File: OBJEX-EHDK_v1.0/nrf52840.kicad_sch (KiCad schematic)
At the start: 21 parts, among them U6 nRF52840, Y2 32MHz, Y3 32.768kHz

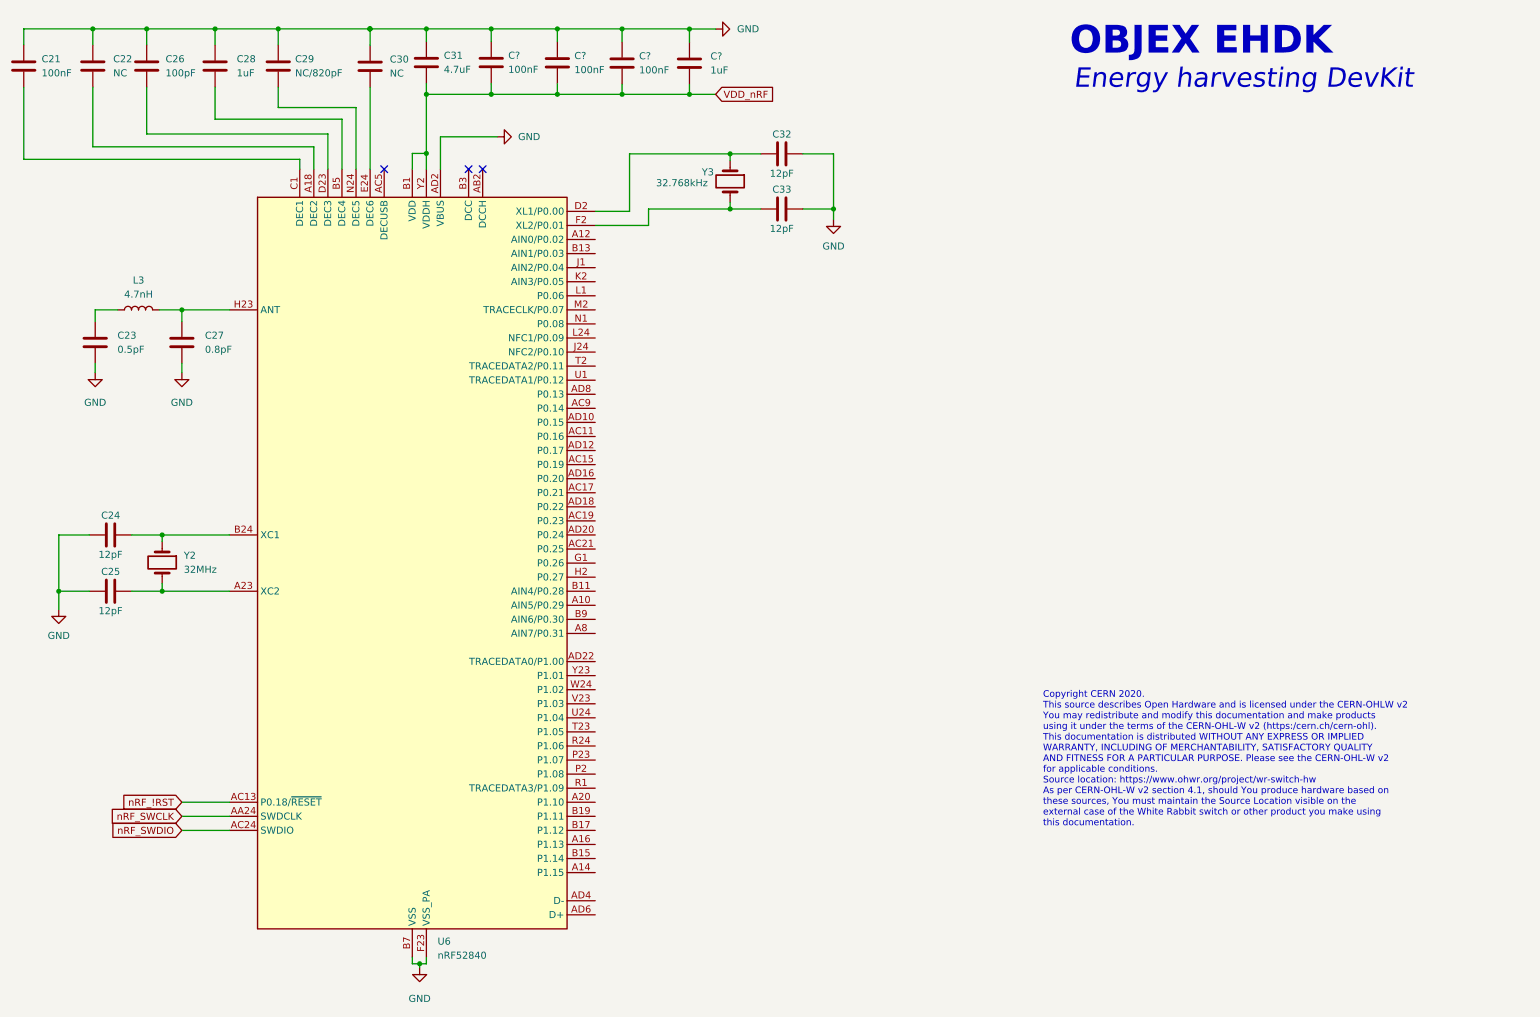
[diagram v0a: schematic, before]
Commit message: add: ADP5091
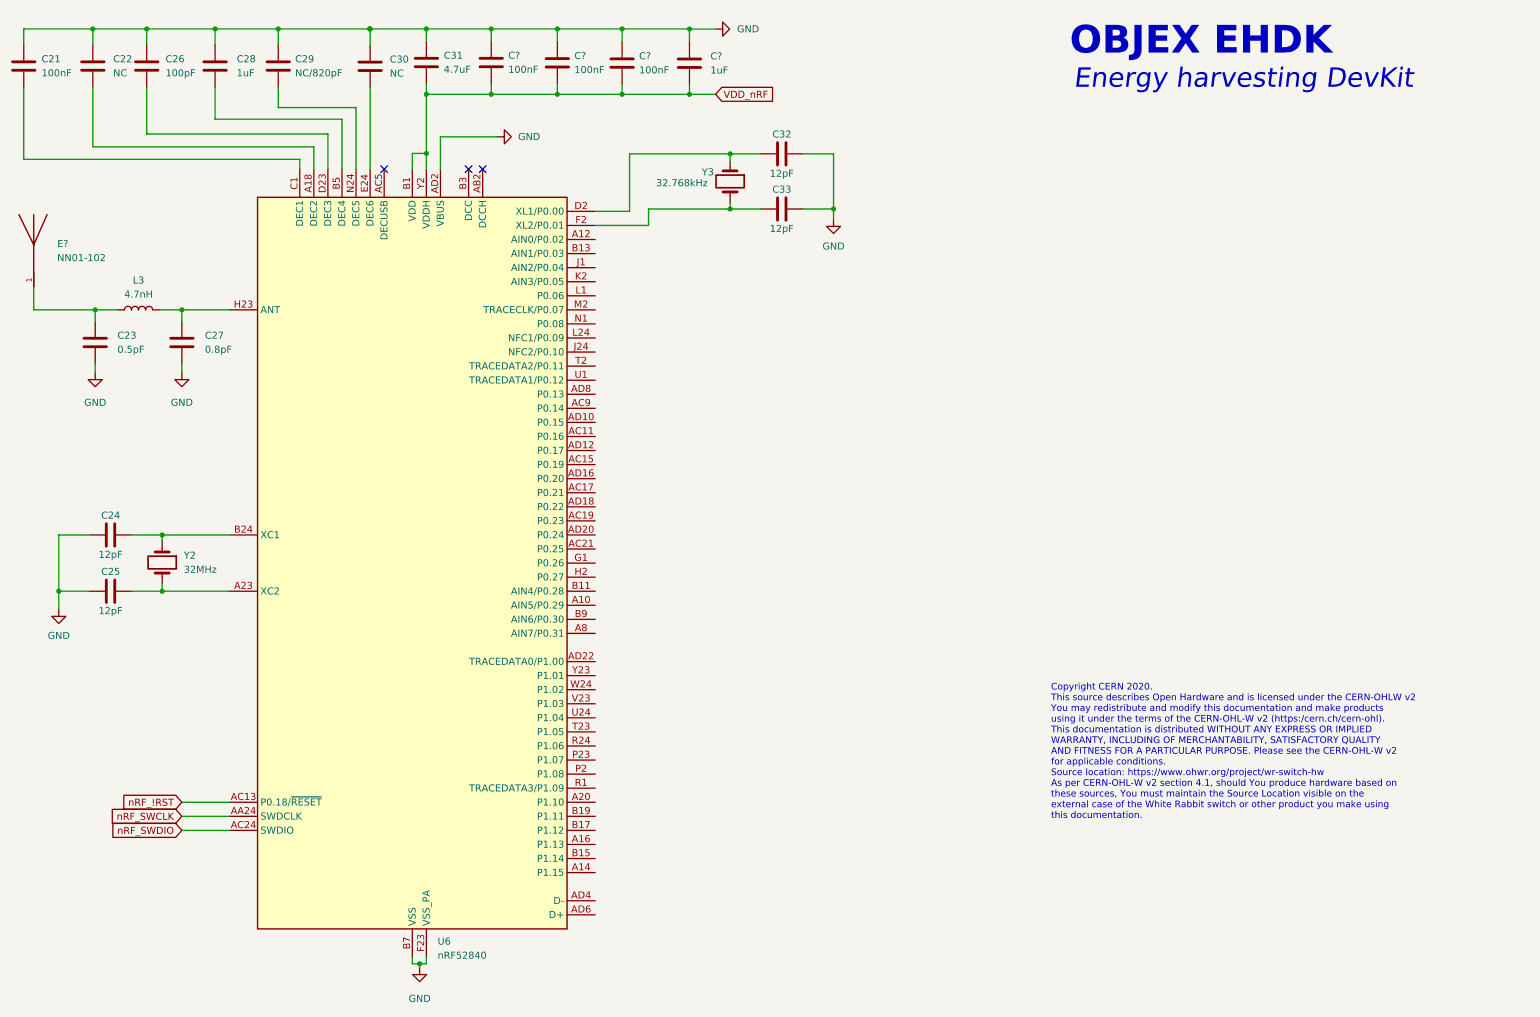
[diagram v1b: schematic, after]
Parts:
- added E?: NN01-102, lib:XCVR_NN01-102, symbol NN01-102:NN01-102
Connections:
- net at C23.1, L3.1: now also E?.1
